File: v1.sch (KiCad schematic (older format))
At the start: 18 parts

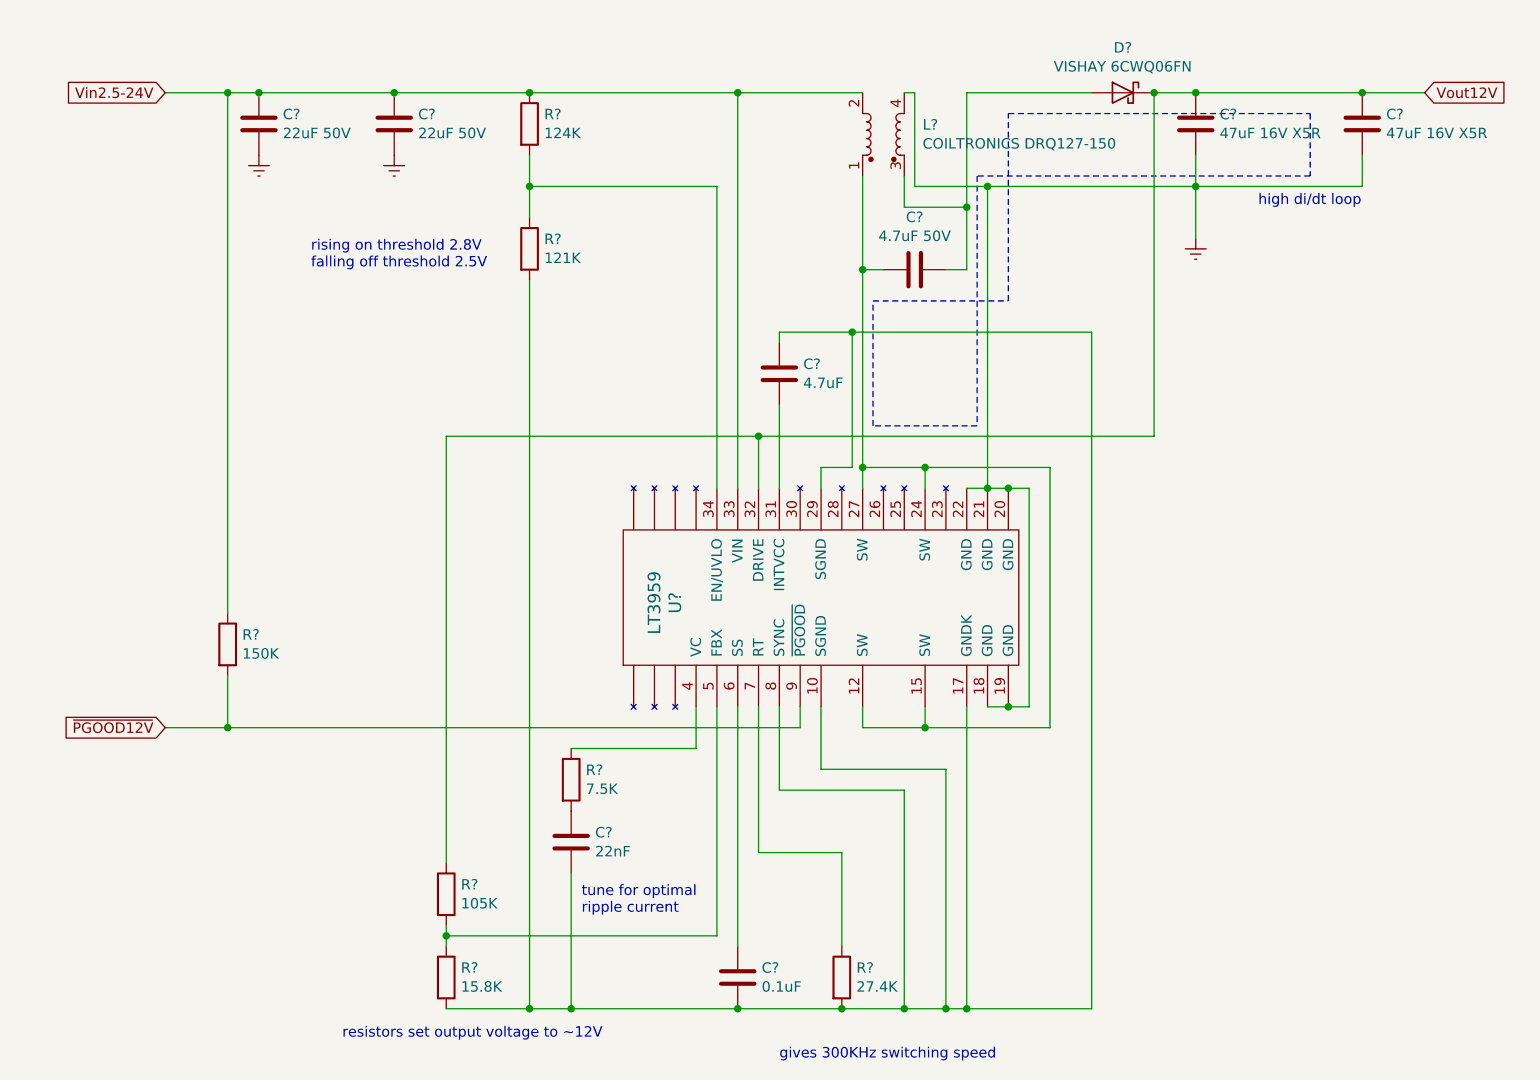
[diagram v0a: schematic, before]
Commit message: Added split inductor symbol
Schematic easier to follow now
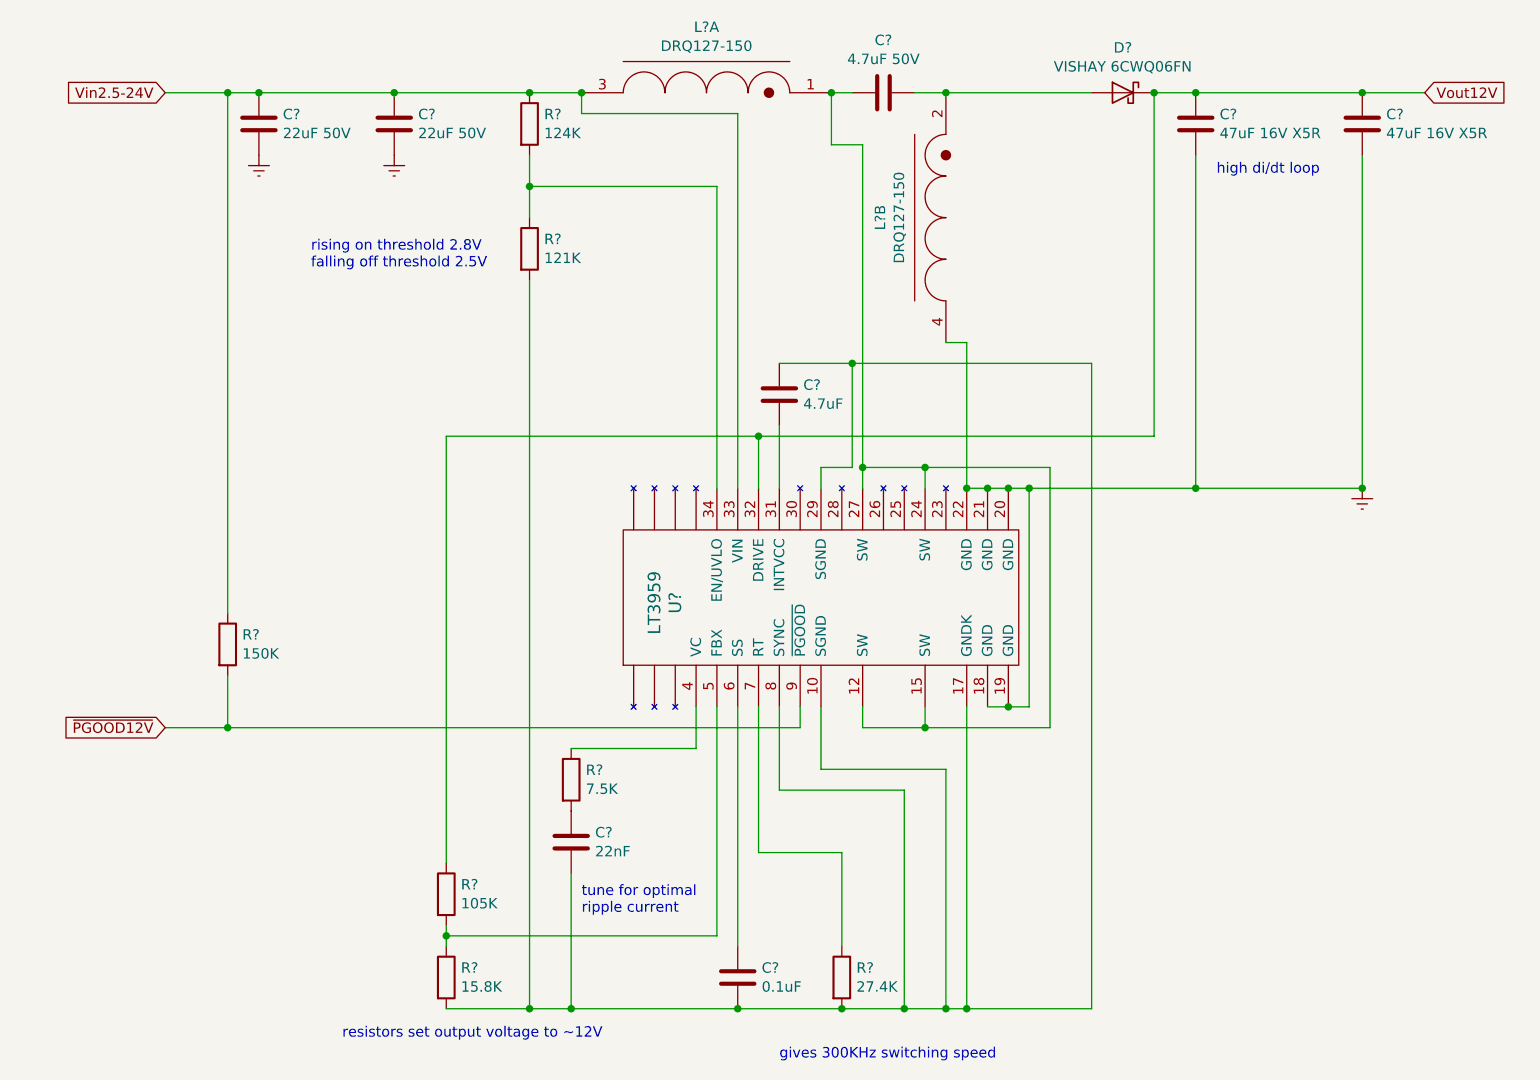
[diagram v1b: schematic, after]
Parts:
- removed L?: COILTRONICS DRQ127-150, symbol Device:L_Coupled
- added L? (x2): DRQ127-150, symbol coiltronics:DRQ127-150
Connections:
- net Earth: now also L?.4
- net Vin2.5-24V: now also L?.3
- net at C?.1, U?.12 (SW), U?.15 (SW)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: now also L?.1
- net at C?.2, D?.2 (A): now also L?.2
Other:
- moved on the sheet: C?
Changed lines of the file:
@@
 L Device:C C?
 U 1 1 5CA3B718
-P 4300 2600
-F 0 "C?" H 4415 2646 50  0000 L CNN
-F 1 "4.7uF" H 4415 2555 50  0000 L CNN
-F 2 "" H 4338 2450 50  0001 C CNN
-F 3 "~" H 4300 2600 50  0001 C CNN
-	1    4300 2600
+P 4300 2700
+F 0 "C?" H 4415 2746 50  0000 L CNN
+F 1 "4.7uF" H 4415 2655 50  0000 L CNN
+F 2 "" H 4338 2550 50  0001 C CNN
+F 3 "~" H 4300 2700 50  0001 C CNN
+	1    4300 2700
 	1    0    0    -1
 $EndComp
@@
 L Device:C C?
 U 1 1 5CA3CF00
-P 4950 2100
-F 0 "C?" V 5202 2100 50  0000 C CNN
-F 1 "4.7uF 50V" V 5111 2100 50  0000 C CNN
-F 2 "" H 4988 1950 50  0001 C CNN
-F 3 "~" H 4950 2100 50  0001 C CNN
-	1    4950 2100
+P 4800 1250
+F 0 "C?" V 5052 1250 50  0000 C CNN
+F 1 "4.7uF 50V" V 4961 1250 50  0000 C CNN
+F 2 "" H 4838 1100 50  0001 C CNN
+F 3 "~" H 4800 1250 50  0001 C CNN
+	1    4800 1250
 	0    -1   -1   0
 $EndComp
@@
 	-1   0    0    -1
 $EndComp
-$Comp
-L Device:L_Coupled L?
-U 1 1 5CA3D989
-P 4800 1450
-F 0 "L?" V 4846 1262 50  0000 R CNN
-F 1 "COILTRONICS DRQ127-150" V 4755 1262 50  0000 R CNN
-F 2 "" H 4800 1450 50  0001 C CNN
-F 3 "~" H 4800 1450 50  0001 C CNN
-	1    4800 1450
-	0    -1   -1   0
-$EndComp
 Wire Wire Line
 	3300 4400 3900 4400
@@
 Connection ~ 2450 1250
 Wire Wire Line
-	3100 1250 4100 1250
-Wire Wire Line
-	4100 1250 4100 3150
-Connection ~ 3100 1250
-Wire Wire Line
-	4100 1250 4700 1250
-Connection ~ 4100 1250
-Wire Wire Line
-	4700 1650 4700 2100
-Wire Wire Line
 	6100 1250 6300 1250
-Wire Wire Line
-	7100 1700 7100 1550
-Wire Wire Line
-	6300 1550 6300 1700
-Connection ~ 6300 1700
-Wire Wire Line
-	6300 1700 7100 1700
 Connection ~ 6300 1250
 Wire Wire Line
@@
 Wire Wire Line
 	1650 4300 1650 4050
-$Comp
-L power:Earth #PWR?
-U 1 1 5CA56ACC
-P 6300 1950
-F 0 "#PWR?" H 6300 1700 50  0001 C CNN
-F 1 "Earth" H 6300 1800 50  0001 C CNN
-F 2 "" H 6300 1950 50  0001 C CNN
-F 3 "~" H 6300 1950 50  0001 C CNN
-	1    6300 1950
-	1    0    0    -1
-$EndComp
-Wire Wire Line
-	6300 1700 6300 1950
 Wire Wire Line
 	2700 5650 3100 5650
@@
 Wire Wire Line
 	5000 3050 5000 3150
-Connection ~ 4700 3050
 Wire Wire Line
 	4700 3050 4700 3150
@@
 	3100 5650 3300 5650
 Wire Wire Line
-	4300 2400 4300 2450
-Wire Wire Line
-	4300 2750 4300 3150
-Wire Wire Line
-	5800 2400 5800 5650
+	5800 2550 5800 5650
 Wire Wire Line
 	5800 5650 5200 5650
@@
 	4900 5650 4600 5650
 Wire Wire Line
-	4300 2400 4650 2400
-Wire Wire Line
 	4500 3150 4500 3050
 Wire Wire Line
 	4500 3050 4650 3050
 Wire Wire Line
-	4650 3050 4650 2400
-Connection ~ 4650 2400
-Wire Wire Line
-	4650 2400 5800 2400
+	4650 3050 4650 2550
+Wire Wire Line
+	4650 2550 5800 2550
 Text GLabel 7400 1250 2    50   Input ~ 0
 Vout12V
@@
 Vin2.5-24V
 Wire Wire Line
-	4700 2100 4800 2100
-Connection ~ 4700 2100
-Wire Wire Line
-	4700 2100 4700 3050
-Wire Wire Line
-	5100 2100 5200 2100
-Wire Wire Line
-	5200 2100 5200 1800
-Wire Wire Line
-	5200 1250 5800 1250
-Wire Wire Line
-	4950 1700 4950 1250
-Wire Wire Line
-	4950 1250 4900 1250
-Wire Wire Line
-	4900 1800 5200 1800
-Wire Wire Line
-	4900 1650 4900 1800
-Connection ~ 5200 1800
-Wire Wire Line
-	5200 1800 5200 1250
-Wire Wire Line
-	4200 2900 6100 2900
-Wire Wire Line
 	6100 2900 6100 1250
 Connection ~ 4200 2900
 Connection ~ 6100 1250
-Wire Notes Line
-	4750 2250 5400 2250
-Wire Notes Line
-	5400 2250 5400 1350
-Wire Notes Line
-	5400 1350 6850 1350
-Wire Notes Line
-	6850 1350 6850 1650
-Wire Notes Line
-	6850 1650 5250 1650
-Text Notes 6600 1800 0    50   ~ 0
+Text Notes 6400 1650 0    50   ~ 0
 high di/dt loop
-Wire Notes Line
-	5250 2850 4750 2850
-Wire Notes Line
-	4750 2850 4750 2250
-Wire Notes Line
-	5250 1650 5250 2850
-Wire Wire Line
-	5300 1700 4950 1700
-Wire Wire Line
-	6300 1700 5300 1700
-Connection ~ 5300 1700
-Wire Wire Line
-	5300 1700 5300 3150
+$Comp
+L coiltronics:DRQ127-150 L?
+U 1 1 5CAC7253
+P 3950 1000
+F 0 "L?" H 3950 1065 50  0000 C CNN
+F 1 "DRQ127-150" H 3950 974 50  0000 C CNN
+F 2 "" H 3950 1000 50  0001 C CNN
+F 3 "" H 3950 1000 50  0001 C CNN
+	1    3950 1000
+	1    0    0    -1
+$EndComp
+Wire Wire Line
+	3100 1250 3350 1250
+Connection ~ 3100 1250
+Wire Wire Line
+	4550 1250 4650 1250
+Wire Wire Line
+	3350 1250 3350 1350
+Wire Wire Line
+	3350 1350 4100 1350
+Wire Wire Line
+	4100 1350 4100 3150
+Connection ~ 3350 1250
+Wire Wire Line
+	4550 1250 4550 1500
+Wire Wire Line
+	4550 1500 4700 1500
+Wire Wire Line
+	4700 1500 4700 3050
+Connection ~ 4550 1250
+Connection ~ 4700 3050
+$Comp
+L coiltronics:DRQ127-150 L?
+U 2 1 5CAE6147
+P 4850 1850
+F 0 "L?" H 4850 1915 50  0000 C CNN
+F 1 "DRQ127-150" H 4850 1824 50  0000 C CNN
+F 2 "" H 4850 1850 50  0001 C CNN
+F 3 "" H 4850 1850 50  0001 C CNN
+	2    4850 1850
+	0    -1   -1   0
+$EndComp
+Wire Wire Line
+	4950 1250 5100 1250
+Wire Wire Line
+	5100 1250 5800 1250
+Connection ~ 5100 1250
+Wire Wire Line
+	5100 2450 5200 2450
+Wire Wire Line
+	5200 2450 5200 3150
+Connection ~ 5200 3150
+Wire Wire Line
+	5500 3150 6300 3150
+Wire Wire Line
+	7100 1550 7100 3150
+Connection ~ 5500 3150
+Wire Wire Line
+	6300 1550 6300 3150
+Connection ~ 6300 3150
+Wire Wire Line
+	6300 3150 7100 3150
+Wire Wire Line
+	4200 2900 6100 2900
+Wire Wire Line
+	4300 2850 4300 3150
+Wire Wire Line
+	4650 2550 4300 2550
+Connection ~ 4650 2550
+$Comp
+L power:Earth #PWR?
+U 1 1 5CB1A9ED
+P 7100 3150
+F 0 "#PWR?" H 7100 2900 50  0001 C CNN
+F 1 "Earth" H 7100 3000 50  0001 C CNN
+F 2 "" H 7100 3150 50  0001 C CNN
+F 3 "~" H 7100 3150 50  0001 C CNN
+	1    7100 3150
+	1    0    0    -1
+$EndComp
+Connection ~ 7100 3150
 $EndSCHEMATC

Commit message: Added footprints, starting layout
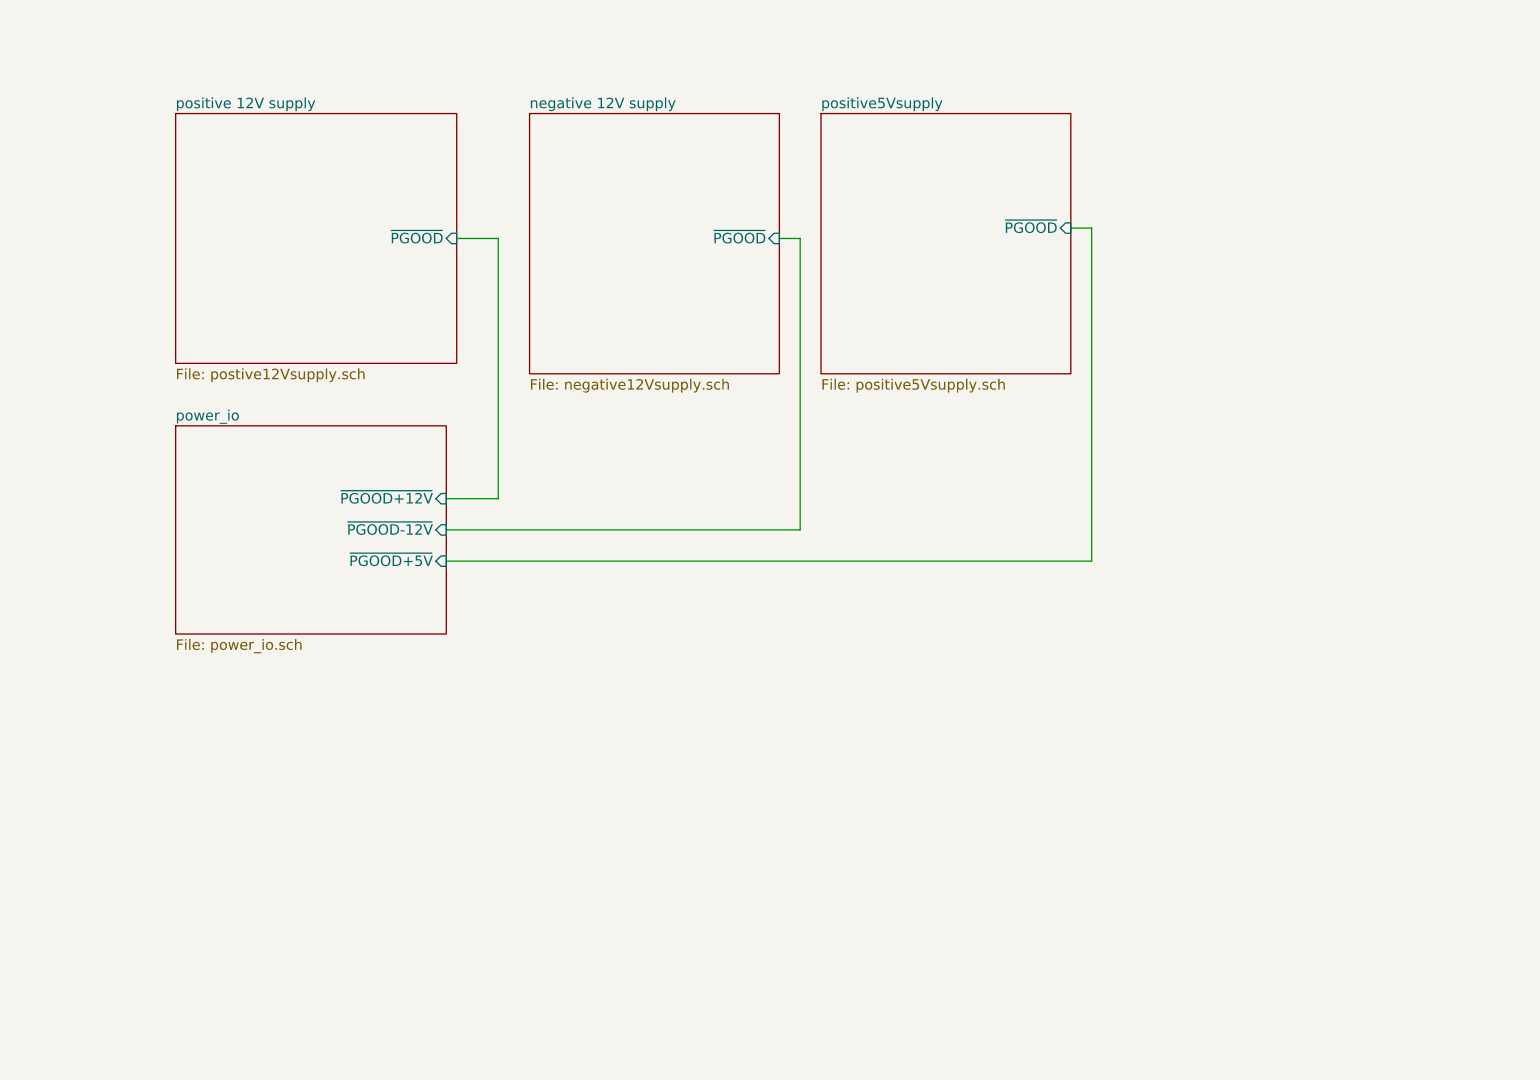
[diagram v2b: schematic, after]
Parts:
- removed C? (x2): 22uF 50V, symbol Device:C
- removed C?: 0.1uF, symbol Device:C
- removed C?: 22nF, symbol Device:C
- removed C?: 4.7uF, symbol Device:C
- removed C?: 4.7uF 50V, symbol Device:C
- removed C? (x2): 47uF 16V X5R, symbol Device:C
- removed D?: VISHAY 6CWQ06FN, symbol Device:D_Schottky
- removed L? (x2): DRQ127-150, symbol coiltronics:DRQ127-150
- removed R?: 150K, symbol Device:R
- removed R?: 124K, symbol Device:R
- removed R?: 121K, symbol Device:R
- removed R?: 27.4K, symbol Device:R
- removed R?: 7.5K, symbol Device:R
- removed R?: 105K, symbol Device:R
- removed R?: 15.8K, symbol Device:R
- removed U?: LT3959, symbol lt3959:LT3959
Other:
- note removed: "gives 300KHz switching speed"
- note removed: "high di/dt loop"
- note removed: "resistors set output voltage to ~~12V"
- note removed: "rising on threshold 2.8V\nfalling off threshold 2.5V"
- note removed: "tune for optimal\nripple current"
